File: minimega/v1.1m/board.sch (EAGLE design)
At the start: 16 parts, among them U1 ATMEGA328P_PDIP, Y1 16MHz

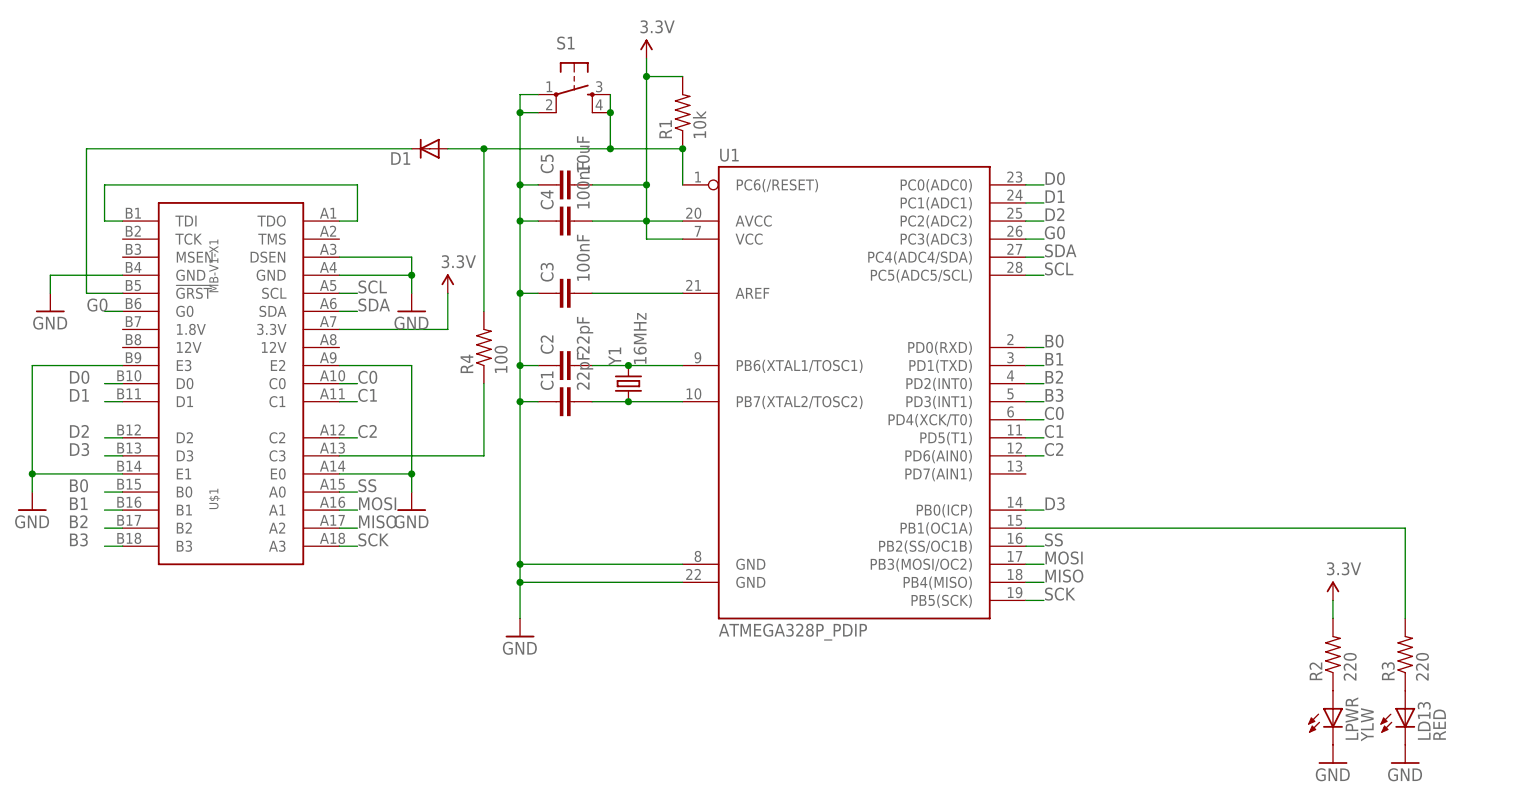
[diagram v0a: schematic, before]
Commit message: rerouted parts of the modboard backplane to put the {2,3}{D,E} lanes on the NC lines
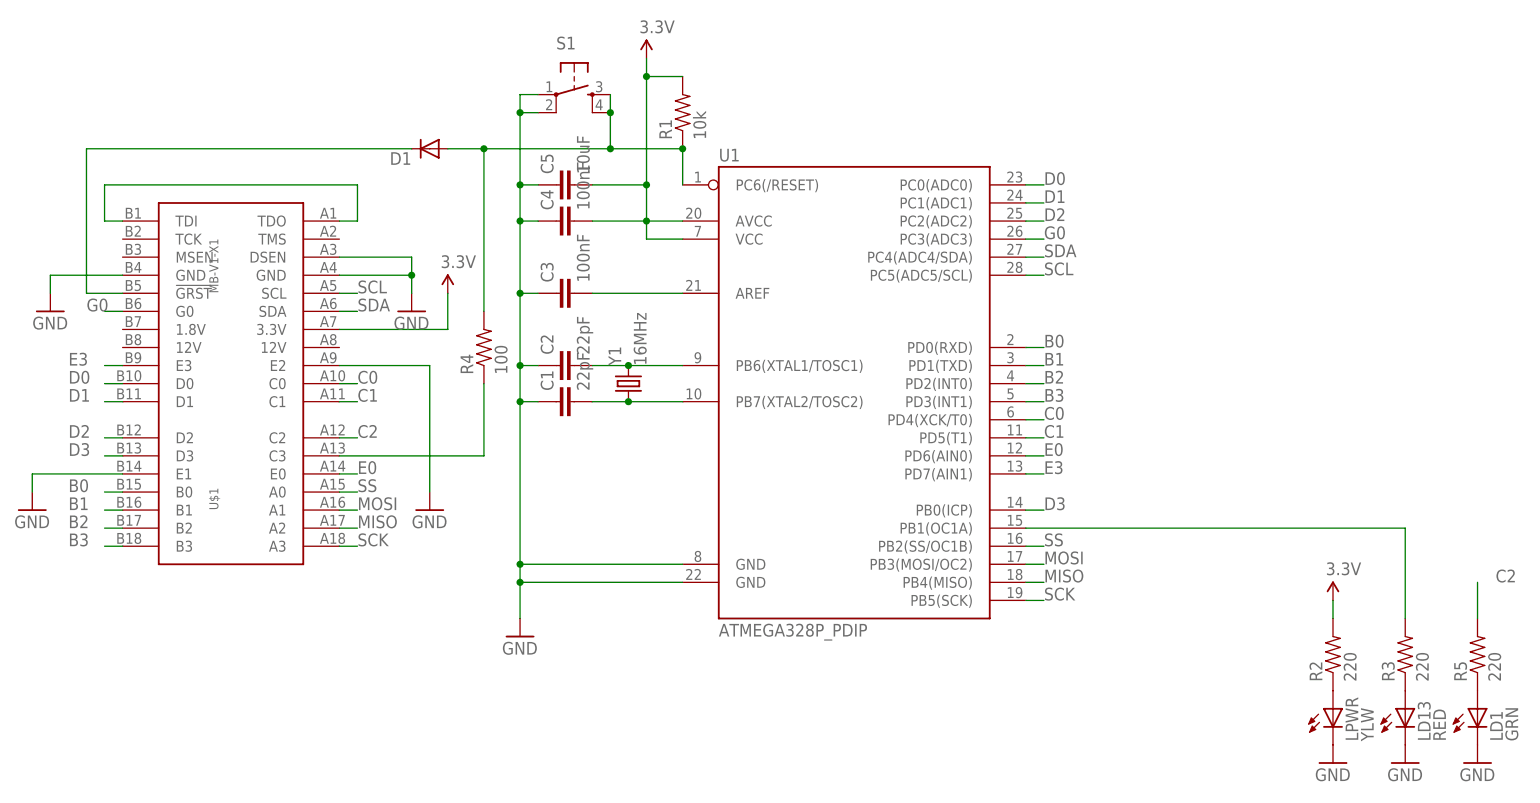
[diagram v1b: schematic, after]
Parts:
- added LD1: GRN, SparkFun-LED:LED-RED0603
- added R5: 220, SparkFun-Resistors:RESISTOR0603
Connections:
- new net E0: U$1.E0, U1.PD6(AIN0)
- new net E3: U$1.E3, U1.PD7(AIN1)
- new net N$7: LD1.A, R5.1
- net C2: now also R5.2; no longer U1.PD6(AIN0)
- net GND: now also LD1.C; no longer U$1.E0, U$1.E3
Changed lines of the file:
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@@
 <part name="GND4" library="kmod-nonparts" deviceset="GND" device=""/>
 <part name="GND5" library="kmod-nonparts" deviceset="GND" device=""/>
+<part name="R5" library="SparkFun-Resistors" deviceset="RESISTOR" device="0603" value="220"/>
+<part name="LD1" library="SparkFun-LED" deviceset="LED-RED" device="0603" value="GRN"/>
+<part name="GND8" library="SparkFun-Aesthetics" deviceset="GND" device=""/>
 </parts>
 <sheets>
@@
 <instance part="R4" gate="G$1" x="-50.8" y="5.08" rot="R90"/>
 <instance part="GND4" gate="1" x="-114.3" y="-17.78"/>
-<instance part="GND5" gate="1" x="-60.96" y="-17.78"/>
+<instance part="GND5" gate="1" x="-58.42" y="-17.78"/>
+<instance part="R5" gate="G$1" x="88.9" y="-38.1" rot="R90"/>
+<instance part="LD1" gate="G$1" x="88.9" y="-45.72"/>
+<instance part="GND8" gate="1" x="88.9" y="-53.34"/>
 </instances>
 <busses>
@@
 </segment>
 <segment>
-<pinref part="U$1" gate="G$1" pin="E3"/>
-<wire x1="-101.6" y1="2.54" x2="-114.3" y2="2.54" width="0.1524" layer="91"/>
-<wire x1="-114.3" y1="2.54" x2="-114.3" y2="-12.7" width="0.1524" layer="91"/>
 <pinref part="U$1" gate="G$1" pin="E1"/>
 <wire x1="-101.6" y1="-12.7" x2="-114.3" y2="-12.7" width="0.1524" layer="91"/>
 <wire x1="-114.3" y1="-12.7" x2="-114.3" y2="-15.24" width="0.1524" layer="91"/>
-<junction x="-114.3" y="-12.7"/>
 <pinref part="GND4" gate="1" pin="GND"/>
 </segment>
 <segment>
-<pinref part="U$1" gate="G$1" pin="E0"/>
-<wire x1="-71.12" y1="-12.7" x2="-60.96" y2="-12.7" width="0.1524" layer="91"/>
-<wire x1="-60.96" y1="-12.7" x2="-60.96" y2="-15.24" width="0.1524" layer="91"/>
 <pinref part="U$1" gate="G$1" pin="E2"/>
-<wire x1="-71.12" y1="2.54" x2="-60.96" y2="2.54" width="0.1524" layer="91"/>
-<wire x1="-60.96" y1="2.54" x2="-60.96" y2="-12.7" width="0.1524" layer="91"/>
-<junction x="-60.96" y="-12.7"/>
+<wire x1="-71.12" y1="2.54" x2="-58.42" y2="2.54" width="0.1524" layer="91"/>
+<wire x1="-58.42" y1="2.54" x2="-58.42" y2="-15.24" width="0.1524" layer="91"/>
 <pinref part="GND5" gate="1" pin="GND"/>
+</segment>
+<segment>
+<pinref part="LD1" gate="G$1" pin="C"/>
+<pinref part="GND8" gate="1" pin="GND"/>
 </segment>
 </net>
@@
 <net name="C2" class="0">
 <segment>
-<pinref part="U1" gate="G$1" pin="PD6(AIN0)"/>
-<wire x1="25.4" y1="-10.16" x2="27.94" y2="-10.16" width="0.1524" layer="91"/>
-<label x="27.94" y="-10.16" size="1.778" layer="95"/>
-</segment>
-<segment>
 <pinref part="U$1" gate="G$1" pin="C2"/>
 <wire x1="-71.12" y1="-7.62" x2="-68.58" y2="-7.62" width="0.1524" layer="91"/>
 <label x="-68.58" y="-7.62" size="1.778" layer="95"/>
+</segment>
+<segment>
+<pinref part="R5" gate="G$1" pin="2"/>
+<wire x1="88.9" y1="-33.02" x2="88.9" y2="-27.94" width="0.1524" layer="91"/>
+<label x="91.44" y="-27.94" size="1.778" layer="95"/>
 </segment>
 </net>
@@
 </segment>
 </net>
+<net name="N$7" class="0">
+<segment>
+<pinref part="R5" gate="G$1" pin="1"/>
+<pinref part="LD1" gate="G$1" pin="A"/>
+</segment>
+</net>
+<net name="E3" class="0">
+<segment>
+<pinref part="U$1" gate="G$1" pin="E3"/>
+<wire x1="-104.14" y1="2.54" x2="-101.6" y2="2.54" width="0.1524" layer="91"/>
+<label x="-109.22" y="2.54" size="1.778" layer="95"/>
+</segment>
+<segment>
+<pinref part="U1" gate="G$1" pin="PD7(AIN1)"/>
+<wire x1="25.4" y1="-12.7" x2="27.94" y2="-12.7" width="0.1524" layer="91"/>
+<label x="27.94" y="-12.7" size="1.778" layer="95"/>
+</segment>
+</net>
+<net name="E0" class="0">
+<segment>
+<pinref part="U$1" gate="G$1" pin="E0"/>
+<wire x1="-71.12" y1="-12.7" x2="-68.58" y2="-12.7" width="0.1524" layer="91"/>
+<label x="-68.58" y="-12.7" size="1.778" layer="95"/>
+</segment>
+<segment>
+<pinref part="U1" gate="G$1" pin="PD6(AIN0)"/>
+<wire x1="25.4" y1="-10.16" x2="27.94" y2="-10.16" width="0.1524" layer="91"/>
+<label x="27.94" y="-10.16" size="1.778" layer="95"/>
+</segment>
+</net>
